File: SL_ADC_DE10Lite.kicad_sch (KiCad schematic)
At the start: 17 parts, among them J1 Conn_02x20_Odd_Even, J2 Conn_01x10, J3 Conn_01x08, J4 Conn_01x08, J5 Conn_01x06

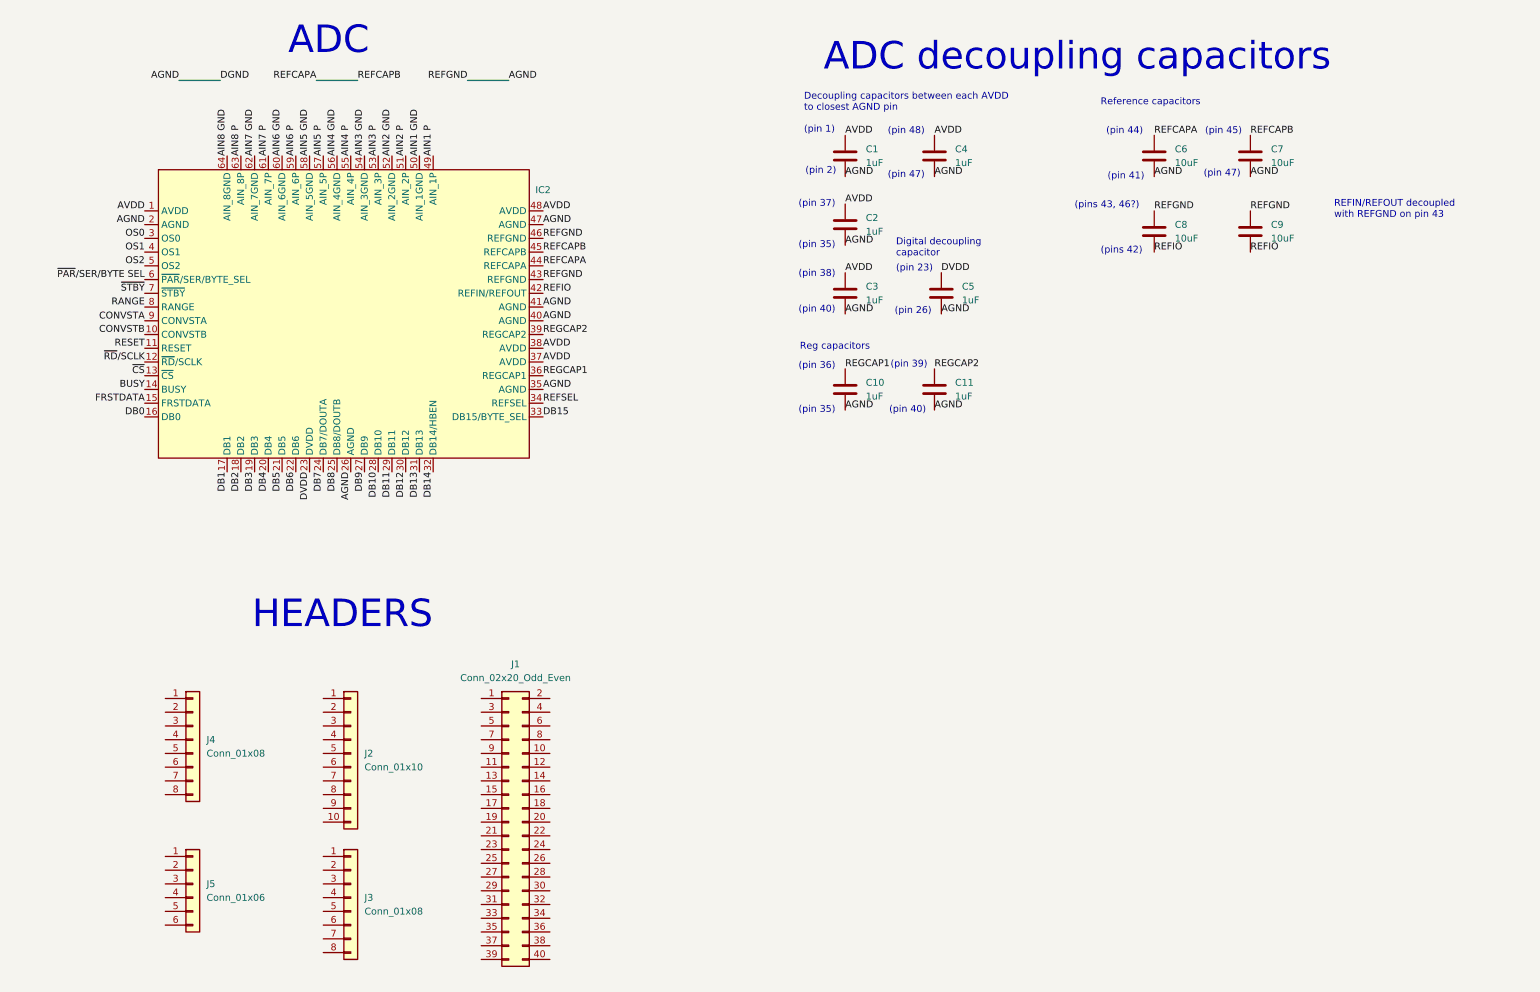
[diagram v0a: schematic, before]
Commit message: Changes to decoupling capacitors
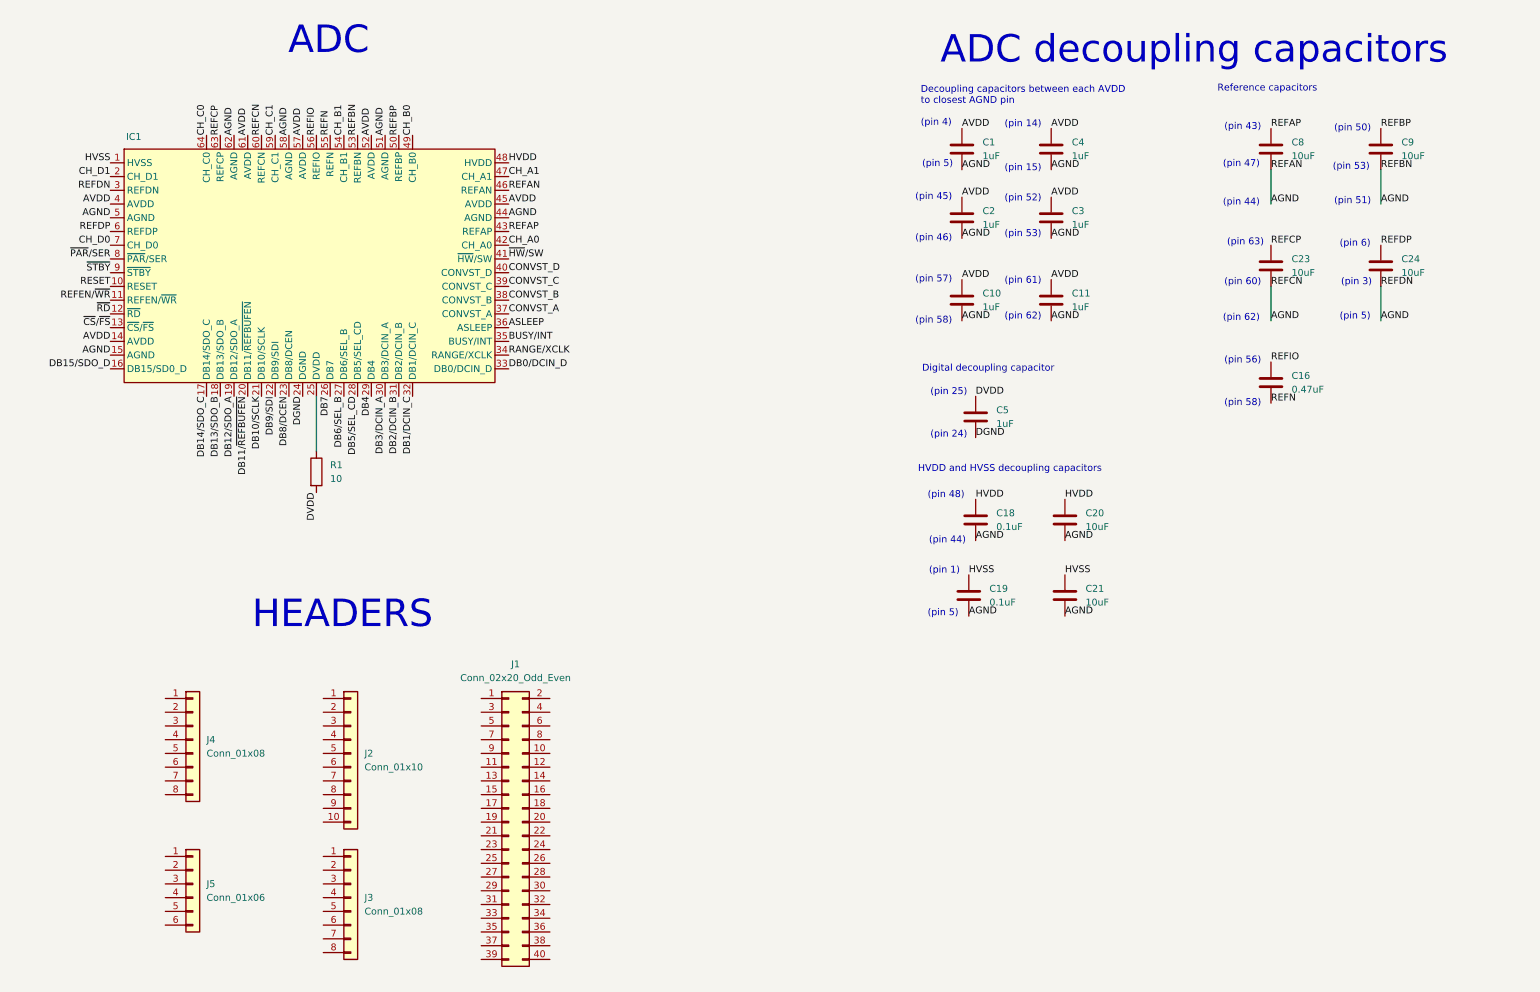
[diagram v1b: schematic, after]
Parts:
- removed C6, C7: 10uF, Capacitor_SMD:C_0805_2012Metric_Pad1.18x1.45mm_HandSolder, symbol Device:C
- removed IC2: (no value), Package_QFP:TQFP-64_10x10mm_P0.5mm, symbol KiCad components:ADS8528SPM
- added C16: 0.47uF, Capacitor_SMD:C_0805_2012Metric_Pad1.18x1.45mm_HandSolder, symbol Device:C
- added C18, C19: 0.1uF, Capacitor_SMD:C_0805_2012Metric_Pad1.18x1.45mm_HandSolder, symbol Device:C
- added C20, C21, C23, C24: 10uF, Capacitor_SMD:C_0805_2012Metric_Pad1.18x1.45mm_HandSolder, symbol Device:C
- added IC1: (no value), Package_QFP:TQFP-64_10x10mm_P0.5mm, symbol KiCad components:ADS8528SPM
- added R1: 10, symbol Device:R
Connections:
- net REGCAP1 is gone; now on net AVDD: C10.1
- net REGCAP2 is gone; now on net AVDD: C11.1
- net AGND: now also C8.2, C9.2, C18.2, C19.2, C20.2, C21.2, C23.2, C24.2, IC1.15 (AGND), IC1.3 (REFDN), IC1.44 (AGND), IC1.46 (REFAN), IC1.5 (AGND), IC1.51 (AGND), IC1.53 (REFBN), IC1.58 (AGND), IC1.60 (REFCN), IC1.62 (AGND); no longer C5.2, C8.1, C9.1
- net AVDD: now also IC1.14 (AVDD), IC1.4 (AVDD), IC1.45 (AVDD), IC1.52 (AVDD), IC1.57 (AVDD), IC1.61 (AVDD)
- net DB4: now also IC1.29 (DB4)
- net DB7: now also IC1.26 (DB7)
- net DVDD: now also R1.2
- net REFIO: now also C16.1, IC1.56 (REFIO); no longer C8.2, C9.2
- net RESET: now also IC1.10 (RESET)
- new net: IC1.25 (DVDD), R1.1
- new net ASLEEP: IC1.36 (ASLEEP)
- new net BUSY/INT: IC1.35 (BUSY/INT)
- new net CH_A0: IC1.42 (CH_A0)
- new net CH_A1: IC1.47 (CH_A1)
- new net CH_B0: IC1.49 (CH_B0)
- new net CH_B1: IC1.54 (CH_B1)
- new net CH_C0: IC1.64 (CH_C0)
- new net CH_C1: IC1.59 (CH_C1)
- new net CH_D0: IC1.7 (CH_D0)
- new net CH_D1: IC1.2 (CH_D1)
- new net CONVST_A: IC1.37 (CONVST_A)
- new net CONVST_B: IC1.38 (CONVST_B)
- new net CONVST_C: IC1.39 (CONVST_C)
- new net CONVST_D: IC1.40 (CONVST_D)
- new net DB0/DCIN_D: IC1.33 (DB0/DCIN_D)
- new net DB10/SCLK: IC1.21 (DB10/SCLK)
- new net DB11/~{REFBUFEN}: IC1.20 (DB11/~{REFBUFEN})
- new net DB12/SDO_A: IC1.19 (DB12/SDO_A)
- new net DB13/SDO_B: IC1.18 (DB13/SDO_B)
- new net DB14/SDO_C: IC1.17 (DB14/SDO_C)
- new net DB15/SDO_D: IC1.16 (DB15/SD0_D)
- new net DB1/DCIN_C: IC1.32 (DB1/DCIN_C)
- new net DB2/DCIN_B: IC1.31 (DB2/DCIN_B)
- new net DB3/DCIN_A: IC1.30 (DB3/DCIN_A)
- new net DB5/SEL_CD: IC1.28 (DB5/SEL_CD)
- new net DB6/SEL_B: IC1.27 (DB6/SEL_B)
- new net DB8/DCEN: IC1.23 (DB8/DCEN)
- new net DB9/SDI: IC1.22 (DB9/SDI)
- new net DGND: C5.2, IC1.24 (DGND)
- new net HVDD: C18.1, C20.1, IC1.48 (HVDD)
- new net HVSS: C19.1, C21.1, IC1.1 (HVSS)
- new net RANGE/XCLK: IC1.34 (RANGE/XCLK)
- new net REFAP: C8.1, IC1.43 (REFAP)
- new net REFBP: C9.1
- new net REFCP: C23.1, IC1.63 (REFCP)
- new net REFDP: C24.1, IC1.6 (REFDP)
- new net REFEN/~{WR}: IC1.11 (REFEN/~{WR})
- new net REFN: C16.2, IC1.55 (REFN)
- new net ~{CS}/~{FS}: IC1.13 (~{CS}/~{FS})
- new net ~{HW}/SW: IC1.41 (~{HW}/SW)
- new net ~{PAR}/SER: IC1.8 (~{PAR}/SER)
- new net ~{RD}: IC1.12 (~{RD})
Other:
- note added: "(pin 14)"
- note added: "(pin 15)"
- note added: "(pin 24)"
- note added: "(pin 25)"
- note added: "(pin 3)"
- note added: "(pin 4)"
- note added: "(pin 43)"
- note added: "(pin 46)"
- note added: "(pin 5)"
- note added: "(pin 50)"
- note added: "(pin 51)"
- note added: "(pin 52)"
- note added: "(pin 53)"
- note added: "(pin 56)"
- note added: "(pin 57)"
- note added: "(pin 58)"
- note added: "(pin 6)"
- note added: "(pin 60)"
- note added: "(pin 61)"
- note added: "(pin 62)"
- note added: "(pin 63)"
- note added: "HVDD and HVSS decoupling capacitors"
- note removed: "(pin 2)"
- note removed: "(pin 23)"
- note removed: "(pin 26)"
- note removed: "(pin 35)"
- note removed: "(pin 36)"
- note removed: "(pin 37)"
- note removed: "(pin 38)"
- note removed: "(pin 39)"
- note removed: "(pin 40)"
- note removed: "(pin 41)"
- note removed: "(pins 42)"
- note removed: "(pins 43, 46?)"
- note removed: "REFIN/REFOUT decoupled with REFGND on pin 43"
- note removed: "Reg capacitors"
- moved on the sheet: C1, C2, C3, C4, C5

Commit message: Added inner copper layers and capacitor routes
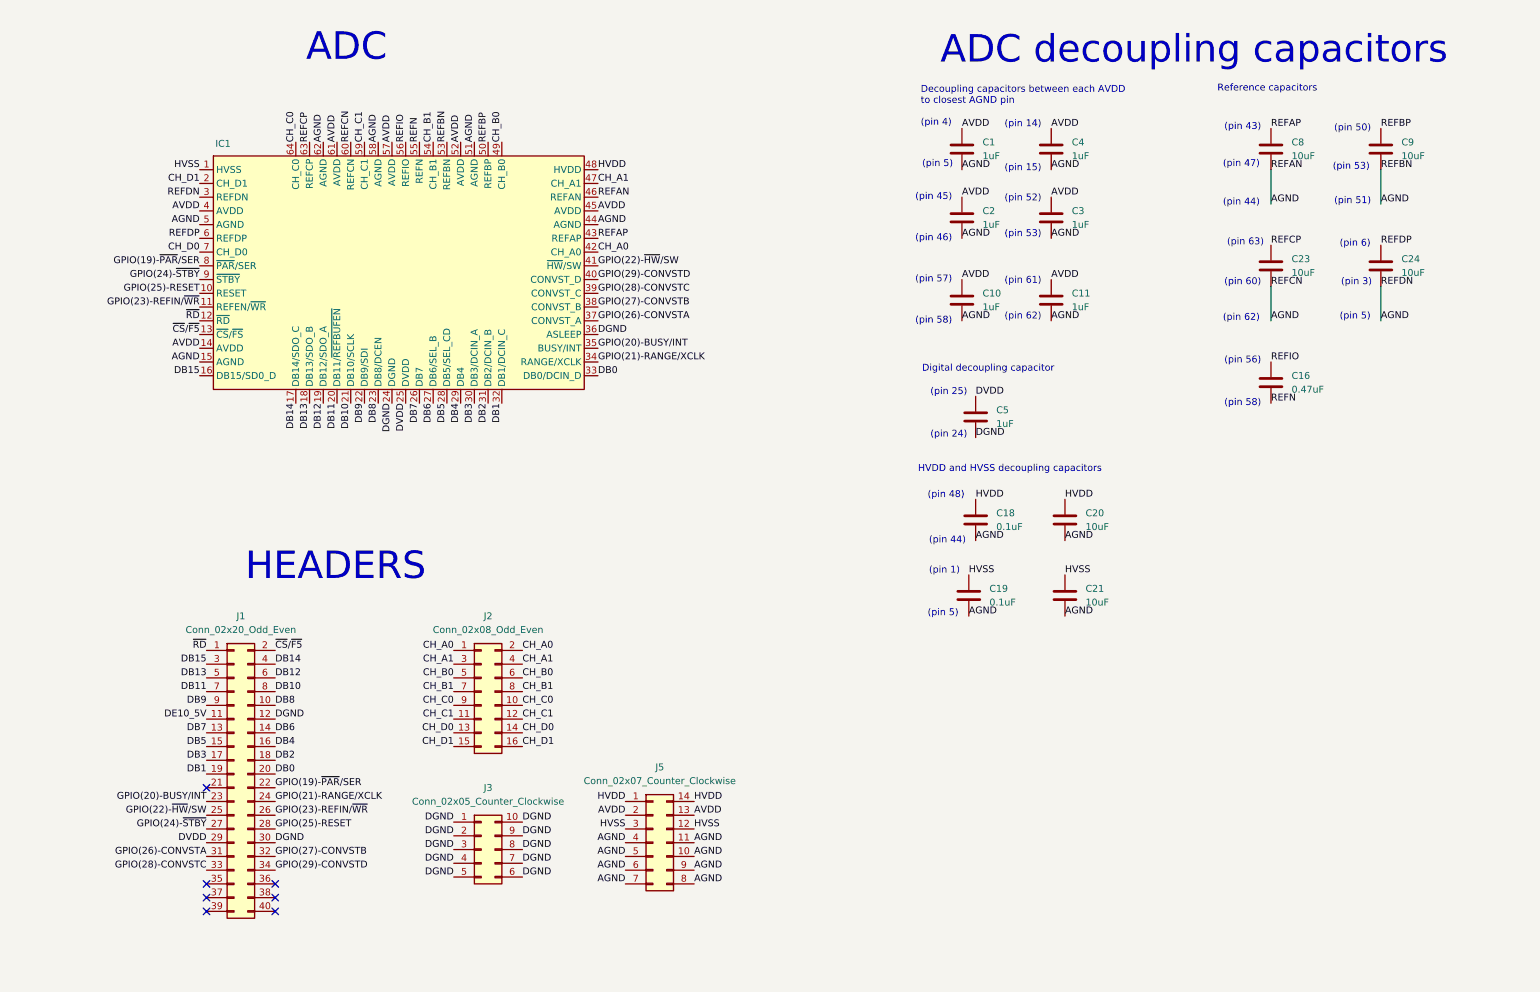
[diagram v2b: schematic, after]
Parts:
- removed J2: Conn_01x10, Connector_PinHeader_2.54mm:PinHeader_1x10_P2.54mm_Vertical, symbol Connector_Generic:Conn_01x10
- removed J3: Conn_01x08, Connector_PinHeader_2.54mm:PinHeader_1x08_P2.54mm_Vertical, symbol Connector_Generic:Conn_01x08
- removed J4: Conn_01x08, symbol Connector_Generic:Conn_01x08
- removed J5: Conn_01x06, Connector_PinHeader_2.54mm:PinHeader_1x06_P2.54mm_Vertical, symbol Connector_Generic:Conn_01x06
- removed R1: 10, symbol Device:R
- added J2: Conn_02x08_Odd_Even, Connector_PinHeader_2.54mm:PinHeader_2x08_P2.54mm_Vertical, symbol Connector_Generic:Conn_02x08_Odd_Even
- added J3: Conn_02x05_Counter_Clockwise, Connector_PinHeader_2.54mm:PinHeader_2x05_P2.54mm_Vertical, symbol Connector_Generic:Conn_02x05_Counter_Clockwise
- added J5: Conn_02x07_Counter_Clockwise, symbol Connector_Generic:Conn_02x07_Counter_Clockwise
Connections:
- net ASLEEP is gone; now on net DGND: IC1.36 (ASLEEP)
- net BUSY/INT is gone; now on net GPIO(20)-BUSY/INT: IC1.35 (BUSY/INT)
- net CONVST_A is gone; now on net GPIO(26)-CONVSTA: IC1.37 (CONVST_A)
- net CONVST_B is gone; now on net GPIO(27)-CONVSTB: IC1.38 (CONVST_B)
- net CONVST_C is gone; now on net GPIO(28)-CONVSTC: IC1.39 (CONVST_C)
- net CONVST_D is gone; now on net GPIO(29)-CONVSTD: IC1.40 (CONVST_D)
- net DB0/DCIN_D is gone; now on net DB0: IC1.33 (DB0/DCIN_D)
- net DB10/SCLK is gone; now on net DB10: IC1.21 (DB10/SCLK)
- net DB11/~{REFBUFEN} is gone; now on net DB11: IC1.20 (DB11/~{REFBUFEN})
- net DB12/SDO_A is gone; now on net DB12: IC1.19 (DB12/SDO_A)
- net DB13/SDO_B is gone; now on net DB13: IC1.18 (DB13/SDO_B)
- net DB14/SDO_C is gone; now on net DB14: IC1.17 (DB14/SDO_C)
- net DB15/SDO_D is gone; now on net DB15: IC1.16 (DB15/SD0_D)
- net DB1/DCIN_C is gone; now on net DB1: IC1.32 (DB1/DCIN_C)
- net DB2/DCIN_B is gone; now on net DB2: IC1.31 (DB2/DCIN_B)
- net DB3/DCIN_A is gone; now on net DB3: IC1.30 (DB3/DCIN_A)
- net DB5/SEL_CD is gone; now on net DB5: IC1.28 (DB5/SEL_CD)
- net DB6/SEL_B is gone; now on net DB6: IC1.27 (DB6/SEL_B)
- net DB8/DCEN is gone; now on net DB8: IC1.23 (DB8/DCEN)
- net DB9/SDI is gone; now on net DB9: IC1.22 (DB9/SDI)
- net RANGE/XCLK is gone; now on net GPIO(21)-RANGE/XCLK: IC1.34 (RANGE/XCLK)
- net REFEN/~{WR} is gone; now on net GPIO(23)-REFIN/~{WR}: IC1.11 (REFEN/~{WR})
- net RESET is gone; now on net GPIO(25)-RESET: IC1.10 (RESET)
- net ~{CS}/~{FS} is gone; now on net ~{CS}/~{F5}: IC1.13 (~{CS}/~{FS})
- net ~{HW}/SW is gone; now on net GPIO(22)-~{HW}/SW: IC1.41 (~{HW}/SW)
- net ~{PAR}/SER is gone; now on net GPIO(19)-~{PAR}/SER: IC1.8 (~{PAR}/SER)
- net AGND: now also J5.10 (Pin_10), J5.11 (Pin_11), J5.4 (Pin_4), J5.5 (Pin_5), J5.6 (Pin_6), J5.7 (Pin_7), J5.8 (Pin_8), J5.9 (Pin_9); no longer IC1.51 (AGND)
- net AVDD: now also J5.13 (Pin_13), J5.2 (Pin_2)
- net CH_A0: now also J2.1 (Pin_1), J2.2 (Pin_2)
- net CH_A1: now also J2.3 (Pin_3), J2.4 (Pin_4)
- net CH_B0: now also J2.5 (Pin_5), J2.6 (Pin_6)
- net CH_B1: now also J2.7 (Pin_7), J2.8 (Pin_8)
- net CH_C0: now also J2.10 (Pin_10), J2.9 (Pin_9)
- net CH_C1: now also J2.11 (Pin_11), J2.12 (Pin_12)
- net CH_D0: now also J2.13 (Pin_13), J2.14 (Pin_14)
- net CH_D1: now also J2.15 (Pin_15), J2.16 (Pin_16)
- net DB4: now also J1.16 (Pin_16)
- net DB7: now also J1.13 (Pin_13)
- net DGND: now also J1.12 (Pin_12), J1.30 (Pin_30), J3.1 (Pin_1), J3.10 (Pin_10), J3.2 (Pin_2), J3.3 (Pin_3), J3.4 (Pin_4), J3.5 (Pin_5), J3.6 (Pin_6), J3.7 (Pin_7), J3.8 (Pin_8), J3.9 (Pin_9)
- net DVDD: now also IC1.25 (DVDD), J1.29 (Pin_29)
- net HVDD: now also J5.1 (Pin_1), J5.14 (Pin_14)
- net HVSS: now also J5.12 (Pin_12), J5.3 (Pin_3)
- net REFBP: now also IC1.50 (REFBP)
- net ~{RD}: now also J1.1 (Pin_1)
- net GPIO(24)-~{STBY}: now reaches IC1.9 (~{STBY})
- net GPIO(24)-~{STBY}: now also J1.27 (Pin_27)
- net DB8: now reaches J1.10 (Pin_10)
- net DE10_5V: now reaches J1.11 (Pin_11)
- net DB6: now reaches J1.14 (Pin_14)
- net DB5: now reaches J1.15 (Pin_15)
- net DB3: now reaches J1.17 (Pin_17)
- net DB2: now reaches J1.18 (Pin_18)
- net DB1: now reaches J1.19 (Pin_19)
- net ~{CS}/~{F5}: now reaches J1.2 (Pin_2)
- net DB0: now reaches J1.20 (Pin_20)
- net GPIO(19)-~{PAR}/SER: now reaches J1.22 (Pin_22)
- net GPIO(20)-BUSY/INT: now reaches J1.23 (Pin_23)
- net GPIO(21)-RANGE/XCLK: now reaches J1.24 (Pin_24)
- net GPIO(22)-~{HW}/SW: now reaches J1.25 (Pin_25)
- net GPIO(23)-REFIN/~{WR}: now reaches J1.26 (Pin_26)
- net GPIO(25)-RESET: now reaches J1.28 (Pin_28)
- net DB15: now reaches J1.3 (Pin_3)
- net GPIO(26)-CONVSTA: now reaches J1.31 (Pin_31)
- net GPIO(27)-CONVSTB: now reaches J1.32 (Pin_32)
- net GPIO(28)-CONVSTC: now reaches J1.33 (Pin_33)
- net GPIO(29)-CONVSTD: now reaches J1.34 (Pin_34)
- net DB14: now reaches J1.4 (Pin_4)
- net DB13: now reaches J1.5 (Pin_5)
- net DB12: now reaches J1.6 (Pin_6)
- net DB11: now reaches J1.7 (Pin_7)
- net DB10: now reaches J1.8 (Pin_8)
- net DB9: now reaches J1.9 (Pin_9)
- no-connect marks 0 -> 7
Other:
- moved on the sheet: IC1, J1
